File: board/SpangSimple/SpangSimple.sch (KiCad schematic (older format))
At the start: 11 parts

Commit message: sending off gerbers
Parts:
- removed R2: R, Resistors_SMD:R_0805_HandSoldering, symbol R
- added D6: D_Schottky, Diodes_SMD:SOD-323_HandSoldering, symbol D_Schottky
- BT1: footprint spang_badge:COINCELL_20MM -> SpangSimple:COINCELL_20MM_HANDSOLDER
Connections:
- net +BATT: now also D6.1 (K); no longer F1.1
- net at D7.1 (K), R1.1: now also D8.1 (K)
- new net: D6.2 (A), F1.1
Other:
- moved on the sheet: BT1, F1, R1
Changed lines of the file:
@@
 L Battery_Cell BT1
 U 1 1 5D564E3C
-P 4250 3650
-F 0 "BT1" H 4350 3750 50  0000 L CNN
-F 1 "Battery_Cell" H 4350 3650 50  0000 L CNN
-F 2 "spang_badge:COINCELL_20MM" V 4250 3710 50  0001 C CNN
-F 3 "" V 4250 3710 50  0000 C CNN
-	1    4250 3650
+P 3850 3650
+F 0 "BT1" H 3950 3750 50  0000 L CNN
+F 1 "Battery_Cell" H 3950 3650 50  0000 L CNN
+F 2 "SpangSimple:COINCELL_20MM_HANDSOLDER" V 3850 3710 50  0001 C CNN
+F 3 "" V 3850 3710 50  0000 C CNN
+	1    3850 3650
 	0    1    1    0
 $EndComp
@@
 L GND #PWR02
 U 1 1 5D5651C5
-P 4000 3700
-F 0 "#PWR02" H 4000 3450 50  0001 C CNN
-F 1 "GND" H 4000 3550 50  0000 C CNN
-F 2 "" H 4000 3700 50  0000 C CNN
-F 3 "" H 4000 3700 50  0000 C CNN
-	1    4000 3700
+P 3600 3700
+F 0 "#PWR02" H 3600 3450 50  0001 C CNN
+F 1 "GND" H 3600 3550 50  0000 C CNN
+F 2 "" H 3600 3700 50  0000 C CNN
+F 3 "" H 3600 3700 50  0000 C CNN
+	1    3600 3700
 	1    0    0    -1
 $EndComp
@@
 L R R1
 U 1 1 5D569EFA
-P 8700 4250
-F 0 "R1" H 8780 4250 50  0000 C CNN
-F 1 "R" V 8700 4250 50  0000 C CNN
-F 2 "Resistors_SMD:R_0805_HandSoldering" V 8630 4250 50  0001 C CNN
-F 3 "" H 8700 4250 50  0000 C CNN
-	1    8700 4250
-	1    0    0    -1
-$EndComp
-$Comp
-L R R2
-U 1 1 5D569F00
-P 9000 4250
-F 0 "R2" V 9080 4250 50  0000 C CNN
-F 1 "R" V 9000 4250 50  0000 C CNN
-F 2 "Resistors_SMD:R_0805_HandSoldering" V 8930 4250 50  0001 C CNN
-F 3 "" H 9000 4250 50  0000 C CNN
-	1    9000 4250
+P 8850 4350
+F 0 "R1" H 8930 4350 50  0000 C CNN
+F 1 "R" V 8850 4350 50  0000 C CNN
+F 2 "Resistors_SMD:R_0805_HandSoldering" V 8780 4350 50  0001 C CNN
+F 3 "" H 8850 4350 50  0000 C CNN
+	1    8850 4350
 	1    0    0    -1
 $EndComp
@@
 L Fuse F1
 U 1 1 5D575861
-P 4700 3650
-F 0 "F1" V 4780 3650 50  0000 C CNN
-F 1 "Fuse" V 4625 3650 50  0000 C CNN
-F 2 "Fuse_Holders_and_Fuses:Fuse_SMD1206_HandSoldering" V 4630 3650 50  0001 C CNN
-F 3 "" H 4700 3650 50  0000 C CNN
-	1    4700 3650
+P 4300 3650
+F 0 "F1" V 4380 3650 50  0000 C CNN
+F 1 "Fuse" V 4225 3650 50  0000 C CNN
+F 2 "Fuse_Holders_and_Fuses:Fuse_SMD1206_HandSoldering" V 4230 3650 50  0001 C CNN
+F 3 "" H 4300 3650 50  0000 C CNN
+	1    4300 3650
 	0    1    1    0
 $EndComp
@@
 	7950 3550 7950 4150
 Wire Wire Line
-	4850 3650 7650 3650
+	4800 3650 7650 3650
 Wire Wire Line
 	7650 3650 7650 4150
@@
 Connection ~ 8250 4900
 Wire Wire Line
-	8700 4050 8700 4100
+	8700 4050 8700 4200
 Wire Wire Line
-	9000 4050 9000 4100
-Wire Wire Line
-	9000 4500 9000 4400
+	9000 4200 9000 4050
 Wire Wire Line
 	8850 3750 8850 3650
 Wire Wire Line
 	8700 3750 9000 3750
-Wire Wire Line
-	8700 4500 9000 4500
-Wire Wire Line
-	8700 4400 8700 4500
 Wire Wire Line
 	8850 4500 8850 4650
@@
 	8250 4900 7050 4900
 Wire Wire Line
-	4000 3700 4000 3650
+	3600 3700 3600 3650
 Wire Wire Line
-	4000 3650 4150 3650
+	3600 3650 3750 3650
 Wire Wire Line
-	4450 3650 4550 3650
+	4050 3650 4150 3650
 Wire Wire Line
 	4950 3600 4950 3650
@@
 Connection ~ 5250 3650
 Connection ~ 5250 3750
+Wire Wire Line
+	8700 4200 9000 4200
+Connection ~ 8850 4200
+$Comp
+L D_Schottky D6
+U 1 1 5DE0A57F
+P 4650 3650
+F 0 "D6" H 4650 3750 50  0000 C CNN
+F 1 "D_Schottky" H 4650 3550 50  0000 C CNN
+F 2 "Diodes_SMD:SOD-323_HandSoldering" H 4650 3650 50  0001 C CNN
+F 3 "" H 4650 3650 50  0000 C CNN
+	1    4650 3650
+	-1   0    0    1
+$EndComp
+Wire Wire Line
+	4450 3650 4500 3650
 $EndSCHEMATC

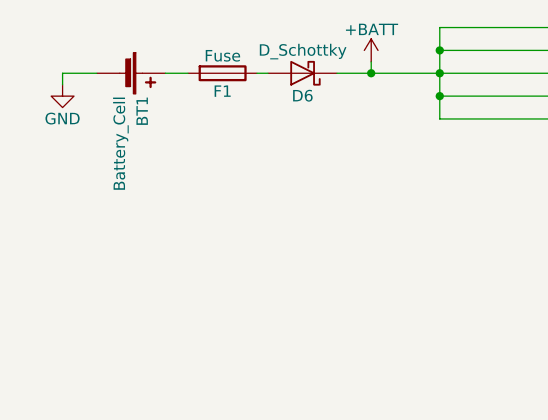
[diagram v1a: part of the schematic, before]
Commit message: removed unecessary fuse, repositioned things on board
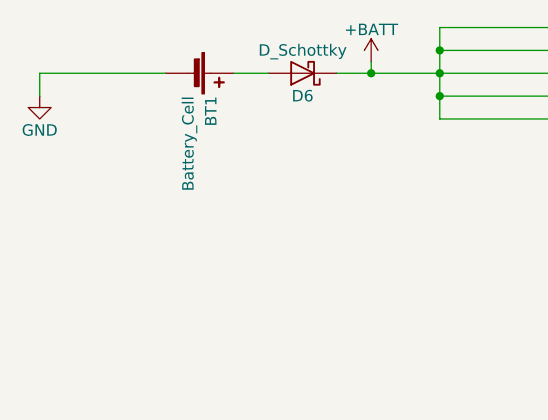
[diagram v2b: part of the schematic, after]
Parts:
- removed F1: Fuse, Fuse_Holders_and_Fuses:Fuse_SMD1206_HandSoldering, symbol Fuse
- D7, D8: footprint SpangSimple:LED_0805_HandSoldering -> SpangSimple:LED_0603_Handsoldering
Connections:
- net at BT1.1 (+): now also D6.2 (A)
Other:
- moved on the sheet: BT1
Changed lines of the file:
@@
 L Battery_Cell BT1
 U 1 1 5D564E3C
-P 3850 3650
-F 0 "BT1" H 3950 3750 50  0000 L CNN
-F 1 "Battery_Cell" H 3950 3650 50  0000 L CNN
-F 2 "SpangSimple:COINCELL_20MM_HANDSOLDER" V 3850 3710 50  0001 C CNN
-F 3 "" V 3850 3710 50  0000 C CNN
-	1    3850 3650
+P 4150 3650
+F 0 "BT1" H 4250 3750 50  0000 L CNN
+F 1 "Battery_Cell" H 4250 3650 50  0000 L CNN
+F 2 "SpangSimple:COINCELL_20MM_HANDSOLDER" V 4150 3710 50  0001 C CNN
+F 3 "" V 4150 3710 50  0000 C CNN
+	1    4150 3650
 	0    1    1    0
 $EndComp
@@
 L GND #PWR02
 U 1 1 5D5651C5
-P 3600 3700
-F 0 "#PWR02" H 3600 3450 50  0001 C CNN
-F 1 "GND" H 3600 3550 50  0000 C CNN
-F 2 "" H 3600 3700 50  0000 C CNN
-F 3 "" H 3600 3700 50  0000 C CNN
-	1    3600 3700
+P 3500 3750
+F 0 "#PWR02" H 3500 3500 50  0001 C CNN
+F 1 "GND" H 3500 3600 50  0000 C CNN
+F 2 "" H 3500 3750 50  0000 C CNN
+F 3 "" H 3500 3750 50  0000 C CNN
+	1    3500 3750
 	1    0    0    -1
 $EndComp
@@
 F 0 "D7" H 8700 4000 50  0000 C CNN
 F 1 "LED" H 8700 3800 50  0000 C CNN
-F 2 "SpangSimple:LED_0805_HandSoldering" H 8700 3900 50  0001 C CNN
+F 2 "SpangSimple:LED_0603_Handsoldering" H 8700 3900 50  0001 C CNN
 F 3 "" H 8700 3900 50  0000 C CNN
 	1    8700 3900
@@
 F 0 "D8" H 9000 4000 50  0000 C CNN
 F 1 "LED" H 9000 3800 50  0000 C CNN
-F 2 "SpangSimple:LED_0805_HandSoldering" H 9000 3900 50  0001 C CNN
+F 2 "SpangSimple:LED_0603_Handsoldering" H 9000 3900 50  0001 C CNN
 F 3 "" H 9000 3900 50  0000 C CNN
 	1    9000 3900
@@
 	1    8850 4650
 	1    0    0    -1
-$EndComp
-$Comp
-L Fuse F1
-U 1 1 5D575861
-P 4300 3650
-F 0 "F1" V 4380 3650 50  0000 C CNN
-F 1 "Fuse" V 4225 3650 50  0000 C CNN
-F 2 "Fuse_Holders_and_Fuses:Fuse_SMD1206_HandSoldering" V 4230 3650 50  0001 C CNN
-F 3 "" H 4300 3650 50  0000 C CNN
-	1    4300 3650
-	0    1    1    0
 $EndComp
 $Comp
@@
 	8250 4900 7050 4900
 Wire Wire Line
-	3600 3700 3600 3650
+	3500 3650 4050 3650
 Wire Wire Line
-	3600 3650 3750 3650
-Wire Wire Line
-	4050 3650 4150 3650
+	4350 3650 4500 3650
 Wire Wire Line
 	4950 3600 4950 3650
@@
 $EndComp
 Wire Wire Line
-	4450 3650 4500 3650
+	3500 3750 3500 3650
 $EndSCHEMATC

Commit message: removed programming stuff, getting ready for final revision. Just needs last checks
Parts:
- added F1: Fuse, Resistors_SMD:R_0603_HandSoldering, symbol Fuse
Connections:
- net GND: now also F1.2; no longer BT1.2 (-)
- new net: BT1.2 (-), F1.1
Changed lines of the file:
@@
 	8250 4900 7050 4900
-Wire Wire Line
-	3500 3650 4050 3650
 Wire Wire Line
 	4350 3650 4500 3650
@@
 Wire Wire Line
 	3500 3750 3500 3650
+$Comp
+L Fuse F1
+U 1 1 5E13951B
+P 3750 3650
+F 0 "F1" V 3830 3650 50  0000 C CNN
+F 1 "Fuse" V 3675 3650 50  0000 C CNN
+F 2 "Resistors_SMD:R_0603_HandSoldering" V 3680 3650 50  0001 C CNN
+F 3 "" H 3750 3650 50  0000 C CNN
+	1    3750 3650
+	0    1    1    0
+$EndComp
+Wire Wire Line
+	3900 3650 4050 3650
+Wire Wire Line
+	3500 3650 3600 3650
 $EndSCHEMATC

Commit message: kfdjkd
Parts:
- removed F1: Fuse, Resistors_SMD:R_0603_HandSoldering, symbol Fuse
- added F1: Polyfuse, Resistors_SMD:R_0603_HandSoldering, symbol Polyfuse
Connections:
- net GND: now also F1.1
- net at BT1.2 (-): now also F1.2
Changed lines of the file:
@@
 Wire Wire Line
 	3500 3750 3500 3650
+Wire Wire Line
+	3800 3650 4050 3650
 $Comp
-L Fuse F1
-U 1 1 5E13951B
-P 3750 3650
-F 0 "F1" V 3830 3650 50  0000 C CNN
-F 1 "Fuse" V 3675 3650 50  0000 C CNN
-F 2 "Resistors_SMD:R_0603_HandSoldering" V 3680 3650 50  0001 C CNN
-F 3 "" H 3750 3650 50  0000 C CNN
-	1    3750 3650
-	0    1    1    0
+L Polyfuse F1
+U 1 1 5E3F2C87
+P 3650 3650
+F 0 "F1" V 3550 3650 50  0000 C CNN
+F 1 "Polyfuse" V 3750 3650 50  0000 C CNN
+F 2 "Resistors_SMD:R_0603_HandSoldering" H 3700 3450 50  0001 L CNN
+F 3 "" H 3650 3650 50  0001 C CNN
+	1    3650 3650
+	0    -1   -1   0
 $EndComp
-Wire Wire Line
-	3900 3650 4050 3650
-Wire Wire Line
-	3500 3650 3600 3650
 $EndSCHEMATC
